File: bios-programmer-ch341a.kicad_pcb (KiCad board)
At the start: 2 copper layers, 50 x 56 mm, 48 parts, among them J1 USB_B_Micro, J4 -Banana-, J5 +Banana+, J6 ZIF16, J7 Conn_02x04_Counter_Clockwise, J8 Conn_02x04_Counter_Clockwise, Q1 IRLML6402, Q2 IRLML6402, Q3 IRLML6402, Q4 IRLML6402, SW1 RESET, U1 CH341A, U2 ISO6741, U3 ADuM1252, U4 TL431DBZ, Y1 12M

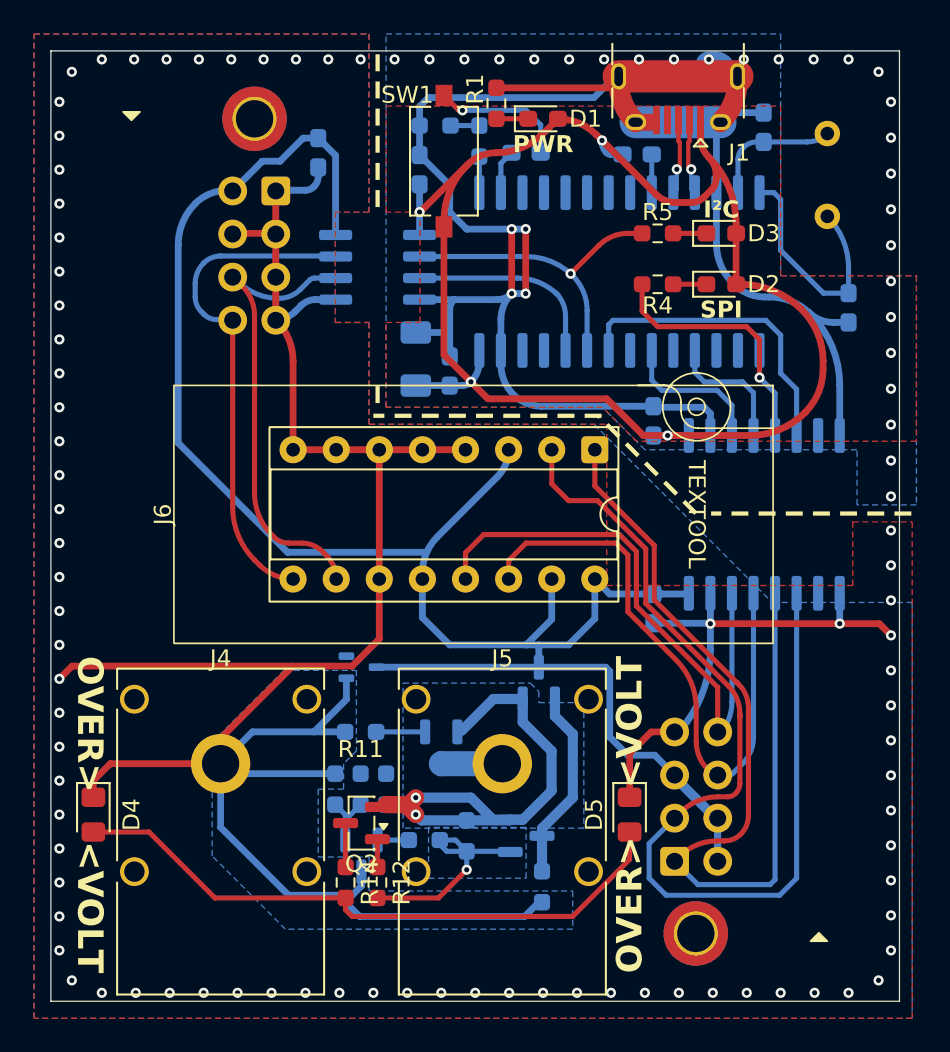
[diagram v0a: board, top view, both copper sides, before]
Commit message: PCB: power path protection reasonable layout TODO
probably final version including power-path protection TODO explain some more? first check previous commit, rebase etc

different mosfet! Toshiba thingy
zones for almost everything
wider tracks
and yeah, accidental symbol ...
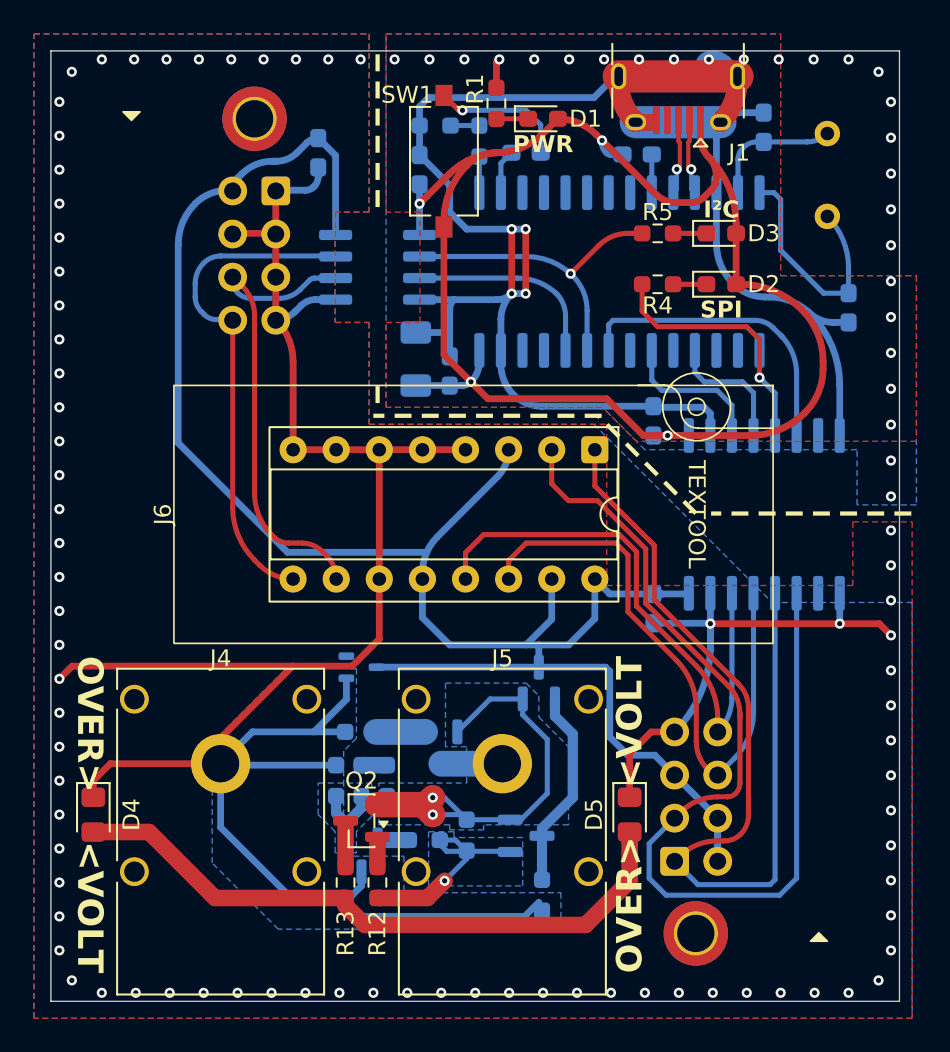
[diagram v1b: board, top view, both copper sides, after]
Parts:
- Q1, Q2, Q3, Q4: value IRLML6402 -> SSM3J328R
- moved R7 0.50 mm to (60.8, 73.0)
- moved R8 0.50 mm to (59.3, 73.0)
- moved R9 0.50 mm to (57.8, 73.0)
- moved R14 0.50 mm to (69.9, 79.8)
- moved Q2 0.14 mm to (59.3, 75.4)
- renumbered R9 to R10, R8 to R11, R14 to R13, R13 to R14, R11 to R6, R6 to R7, R7 to R8, R10 to R9
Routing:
- net GND: track 232.6 -> 226.9 mm
- net VDD: track 118.3 -> 114.7 mm
- net /VSW: track 29.4 -> 27.4 mm
- net VBUS: track 91.6 -> 93.5 mm
- net Net-(R7-Pad1): track 0.00 -> 1.50 mm
- net /OVPLED: track 37.1 -> 38.1 mm
- net /REF431: track 4.80 -> 5.80 mm
- net /SCL_I: track 27.4 -> 28.3 mm
- net /MOSI_I: track 34.0 -> 33.3 mm
- net /CLK_I: track 35.1 -> 34.5 mm
- net GNDD: track 451.2 -> 450.7 mm
- net /VG_MAIN: track 11.3 -> 11.8 mm
- added copper zone on B.Cu, net /REF431

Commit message: diode removed, zones improved, temp commit?
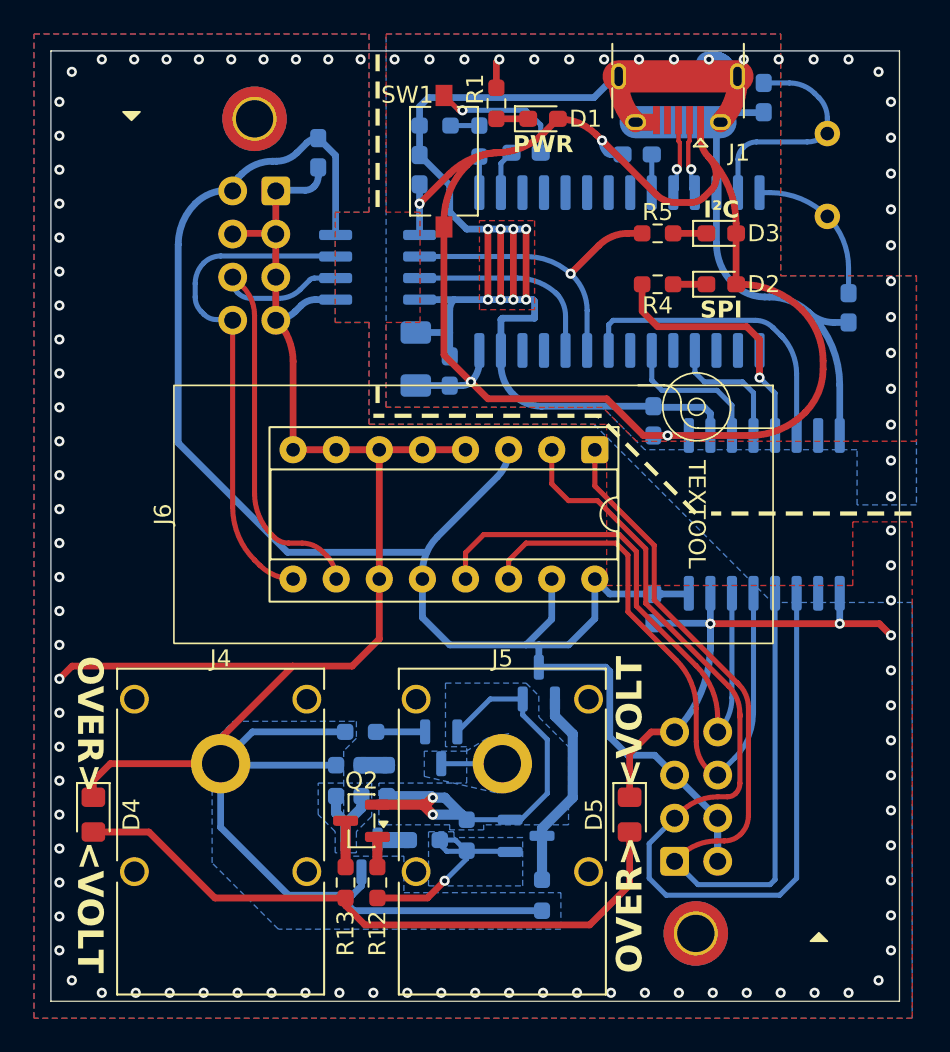
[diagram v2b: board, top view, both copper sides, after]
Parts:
- removed D6: BAT54W, Package_TO_SOT_SMD:SOT-323_SC-70
- moved C1 1.75 mm to (83.0, 32.8), turned to -90 degrees
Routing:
- net GND: track 226.9 -> 237.7 mm, vias 31 -> 35
- net VDD: track 114.7 -> 105.1 mm
- net Net-(U1-XI): track 7.90 -> 13.7 mm
- net Net-(U1-XO): track 14.3 -> 9.18 mm
- net GNDD: track 450.7 -> 446.4 mm
- added copper zone on B.Cu, net /VBJ+
- added copper zone on F.Cu, net GND

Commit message: pcb temp almost done; the only thing I don't like is the GND bridge
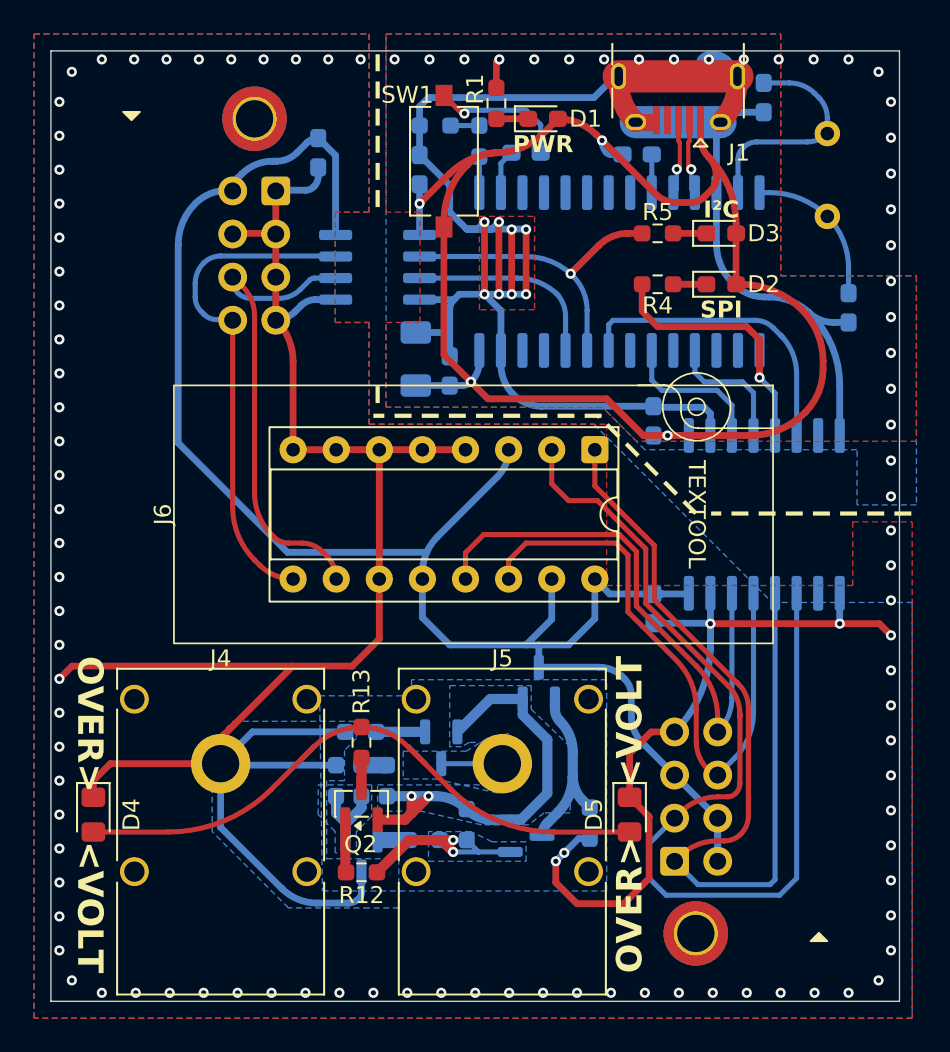
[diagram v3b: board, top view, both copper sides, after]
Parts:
- moved R13 8.30 mm to (59.3, 70.8), turned to 90 degrees
- moved R14 5.10 mm to (72.8, 75.5)
- moved R12 1.11 mm to (59.3, 78.4), turned to 0 degrees
- moved Q2 1.00 mm to (59.3, 74.4), turned to 90 degrees
- moved R10 0.62 mm to (65.5, 75.6)
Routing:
- net GNDD: track 446.4 -> 450.3 mm, vias 76 -> 78
- net /VSW: track 27.4 -> 25.8 mm
- net GND: track 237.7 -> 239.1 mm
- net Net-(Q2-G): track 1.78 -> 3.06 mm
- net Net-(Q2-D): track 2.73 -> 1.76 mm
- net VDD: track 105.1 -> 104.2 mm
- net /VG_AUX: track 13.2 -> 14.1 mm, vias 1 -> 2
- net /VG_MAIN: track 11.8 -> 11.0 mm

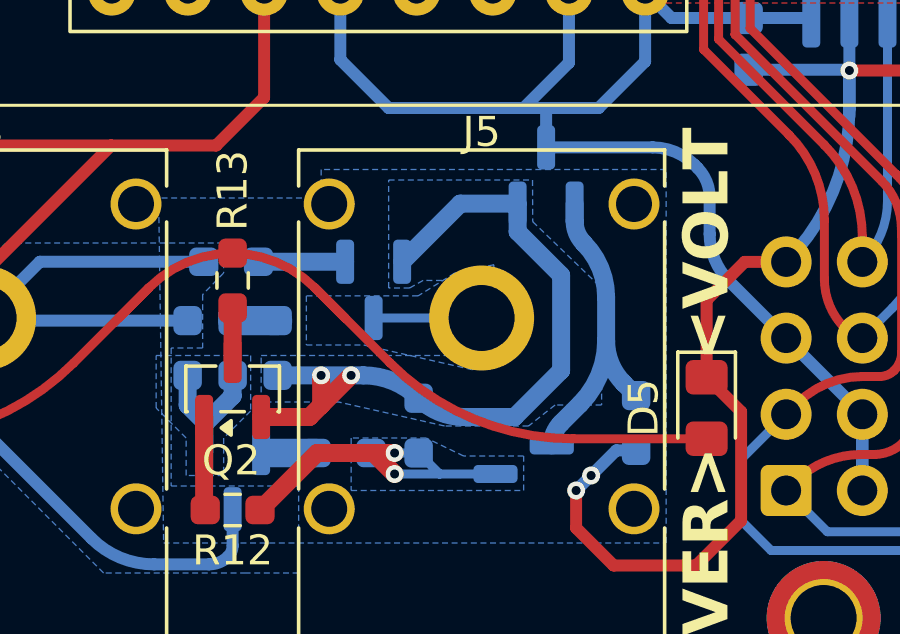
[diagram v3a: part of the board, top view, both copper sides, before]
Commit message: pcb: arc zone turned to tracks
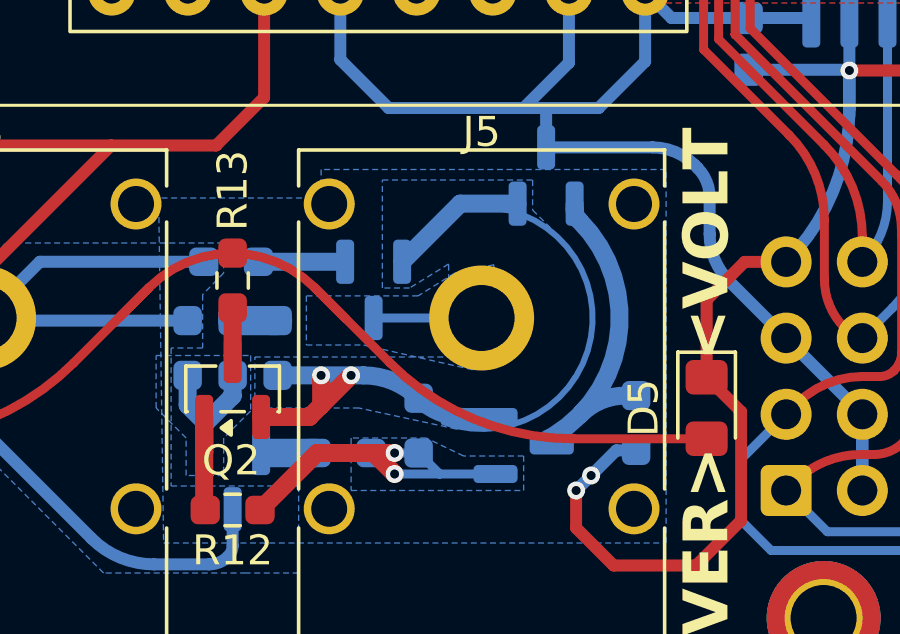
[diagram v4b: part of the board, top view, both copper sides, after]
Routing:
- net /VSW: track 25.8 -> 16.8 mm
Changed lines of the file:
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@@
 		)
 	)
+	(gr_arc
+		(start 67.6 68.3)
+		(mid 71.243789 72.642498)
+		(end 66.334525 75.476863)
+		(stroke
+			(width 0.2)
+			(type solid)
+		)
+		(layer "B.Cu")
+		(net "/VSW")
+	)
 	(gr_poly
 		(pts
@@
 	)
 	(segment
-		(start 68.8 68.1875)
-		(end 68.8 69.125)
-		(width 0.6)
-		(layer "B.Cu")
-		(net "/VSW")
-	)
-	(segment
-		(start 70.25 73.75)
-		(end 68.7 75.3)
-		(width 0.6)
-		(layer "B.Cu")
-		(net "/VSW")
-	)
-	(segment
-		(start 70.25 70.575)
-		(end 70.25 73.75)
-		(width 0.6)
-		(layer "B.Cu")
-		(net "/VSW")
-	)
-	(segment
 		(start 68.0625 75.3)
 		(end 67.008883 75.3)
@@
 		(net "/VSW")
 	)
-	(segment
-		(start 68.7 75.3)
-		(end 68.0625 75.3)
-		(width 0.6)
-		(layer "B.Cu")
-		(net "/VSW")
-	)
-	(segment
-		(start 68.8 69.125)
-		(end 70.25 70.575)
-		(width 0.6)
-		(layer "B.Cu")
-		(net "/VSW")
-	)
 	(arc
 		(start 67.008883 75.3)
@@
 	)
 	(segment
-		(start 72.333318 74.170818)
-		(end 72.75 74.5875)
-		(width 0.6)
-		(layer "B.Cu")
-		(net "/VG_MAIN")
-	)
-	(segment
-		(start 71.75 71.31066)
-		(end 71.75 72.762563)
-		(width 0.6)
-		(layer "B.Cu")
-		(net "/VG_MAIN")
-	)
-	(segment
 		(start 70.7 68.1875)
-		(end 70.7 68.775736)
+		(end 70.7 68.376055)
 		(width 0.6)
 		(layer "B.Cu")
@@
 	)
 	(segment
-		(start 70.24686 75.503139)
-		(end 70.875 74.875)
+		(start 72.75 74.5875)
+		(end 72.389205 74.5875)
 		(width 0.6)
 		(layer "B.Cu")
@@
 	)
 	(arc
-		(start 72.333318 74.170818)
-		(mid 71.901599 73.524705)
-		(end 71.75 72.762563)
+		(start 70.7 68.376055)
+		(mid 70.739883 68.57656)
+		(end 70.85346 68.74654)
 		(width 0.6)
 		(layer "B.Cu")
@@
 	)
 	(arc
-		(start 70.875 74.875)
-		(mid 71.522595 73.905805)
-		(end 71.75 72.762563)
+		(start 72.389205 74.5875)
+		(mid 71.584917 74.747482)
+		(end 70.903075 75.203075)
 		(width 0.6)
 		(layer "B.Cu")
@@
 	)
 	(arc
-		(start 70.24686 75.503139)
-		(mid 70.0179 75.845801)
-		(end 69.9375 76.25)
-		(width 0.6)
-		(layer "B.Cu")
-		(net "/VG_MAIN")
-	)
-	(arc
-		(start 70.7 68.775736)
-		(mid 70.777968 69.167704)
-		(end 71 69.5)
-		(width 0.6)
-		(layer "B.Cu")
-		(net "/VG_MAIN")
-	)
-	(arc
-		(start 71 69.5)
-		(mid 71.555081 70.330738)
-		(end 71.75 71.31066)
+		(start 70.85346 68.74654)
+		(mid 72.127657 72.818734)
+		(end 69.50804 76.186811)
 		(width 0.6)
 		(layer "B.Cu")
@@
 		(polygon
 			(pts
-				(xy 66.598802 70.75) (xy 65.650306 70.747285) (xy 65.19997 71.000025) (xy 64.5 71) (xy 64.5 67.4)
-				(xy 69.296706 67.4) (xy 69.303146 68.789198) (xy 71.598802 71) (xy 71.599445 74.899744) (xy 70.048802 74.9)
-				(xy 69.163323 75.6) (xy 66.366667 75.6) (xy 62.833333 74.8) (xy 60.25 74.8) (xy 60.25 73.25) (xy 66.598802 73.25)
+				(xy 66.5 70.2) (xy 65.2 71.000025) (xy 64.291666 71) (xy 64.291666 67.4) (xy 69.300237 67.400537)
+				(xy 69.29976 68.403953) (xy 70.1 69.2) (xy 70.912952 70.2) (xy 71.3 71.4) (xy 71.2 73.1) (xy 70.1 74.8)
+				(xy 68.4 75.7) (xy 66.75 75.7) (xy 63.508332 75) (xy 60.041666 75) (xy 60.041666 73.3) (xy 66.5 73.3)
 			)
 		)
@@
 			(clearance 0.5)
 		)
-		(min_thickness 0.5)
+		(min_thickness 0.8)
 		(fill yes
 			(thermal_gap 0.5)
-			(thermal_bridge_width 1)
+			(thermal_bridge_width 5)
 			(smoothing fillet)
 			(radius 0.5)

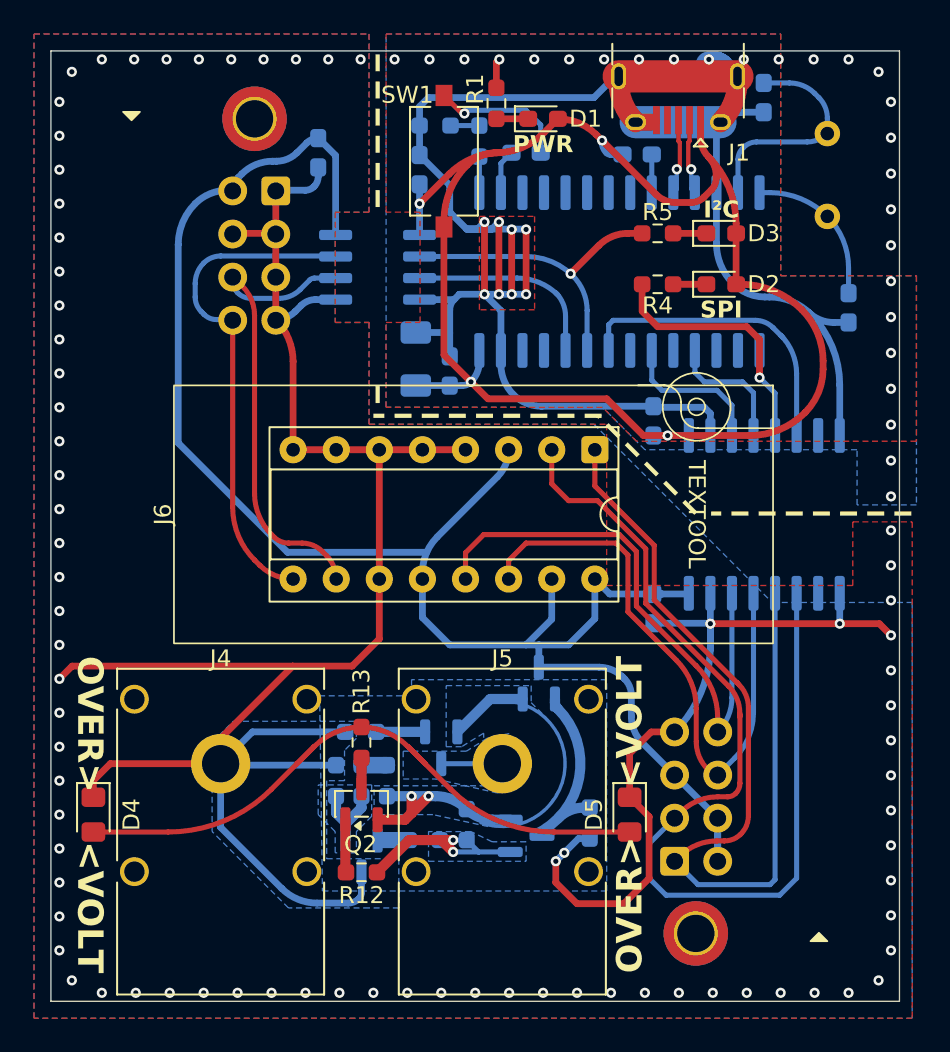
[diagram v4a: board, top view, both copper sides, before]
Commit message: PCB: moved OVP LED tracks down, added LED resistor and some beautification
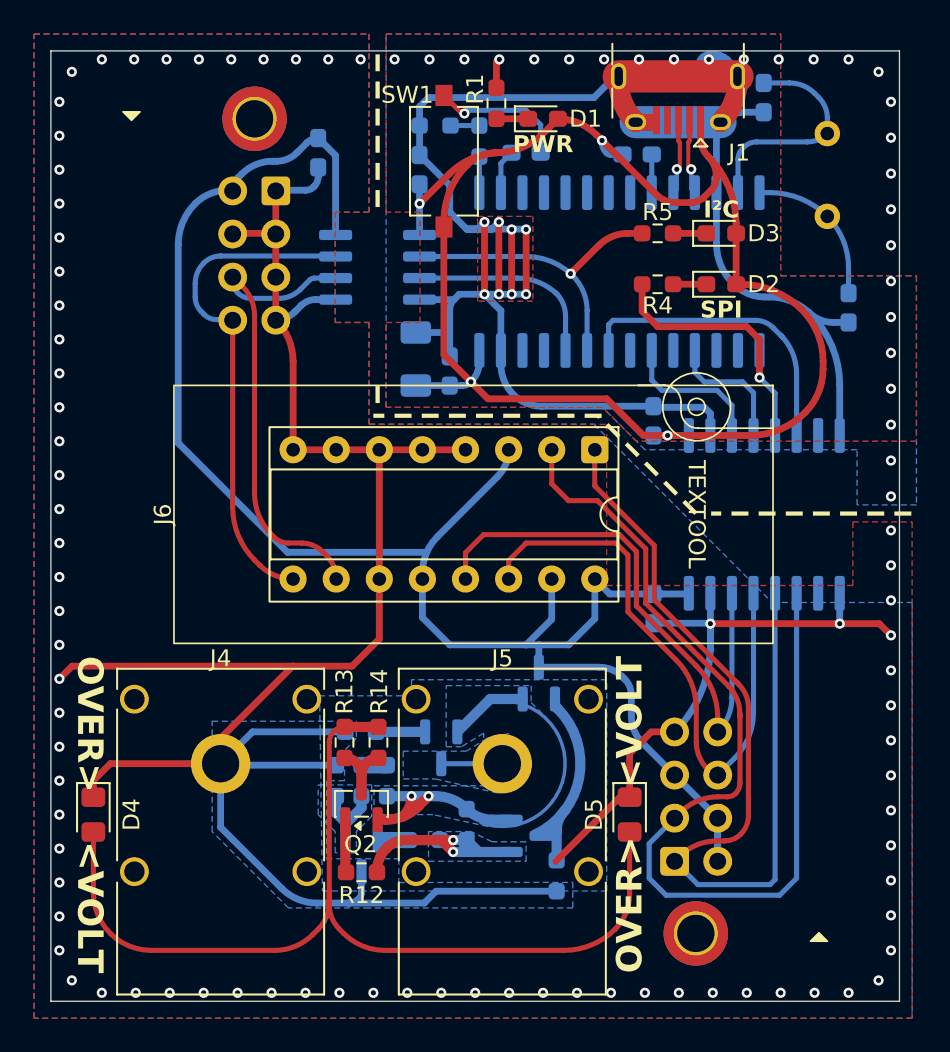
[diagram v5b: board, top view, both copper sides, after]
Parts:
- added R14: 220Ω, Resistor_SMD:R_0603_1608Metric_Pad0.98x0.95mm_HandSolder, F.Cu at (60.3, 70.8)
- moved R15 3.66 mm to (70.8, 78.6)
- moved R13 1.00 mm to (58.3, 70.8), turned to -90 degrees
- renumbered R14 to R15
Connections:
- R13 pad 1: Net-(Q2-D) -> /OVPLED
- R13 pad 2: /OVPLED -> Net-(Q2-D)
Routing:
- net /OVPLED: track 38.4 -> 58.9 mm
- net GNDD: track 450.3 -> 453.1 mm, vias 78 -> 76
- net Net-(Q2-D): track 1.76 -> 3.82 mm
- net /VG_MAIN: track 11.1 -> 12.2 mm
